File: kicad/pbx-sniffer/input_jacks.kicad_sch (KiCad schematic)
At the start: 24 parts

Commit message: commenced placement on pcb
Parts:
- renumbered J7 to J1, J4 to J10, J5 to J11, J6 to J12, J8 to J2, J9 to J3, J10 to J4, J11 to J5, J12 to J6, J1 to J7, J2 to J8, J3 to J9
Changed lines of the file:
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@@
+		(on_board yes)
+		(dnp no)
+		(property "Reference" "J2"
+			(at 81.28 53.34 0)
+			(effects
+				(font
+					(size 1.27 1.27)
+				)
+			)
+		)
+		(property "Value" "~"
+			(at 80.01 52.07 0)
+			(effects
+				(font
+					(size 1.27 1.27)
+				)
+				(hide yes)
+			)
+		)
+		(property "Footprint" "Phones:Molex 0955016649"
+			(at 81.28 54.61 0)
+			(effects
+				(font
+					(size 1.27 1.27)
+				)
+				(hide yes)
+			)
+		)
+		(property "Datasheet" ""
+			(at 81.28 54.61 0)
+			(effects
+				(font
+					(size 1.27 1.27)
+				)
+				(hide yes)
+			)
+		)
+		(property "Description" ""
+			(at 81.28 54.61 0)
+			(effects
+				(font
+					(size 1.27 1.27)
+				)
+				(hide yes)
+			)
+		)
+		(property "DKPN" "WM5574-ND"
+			(at 81.28 54.61 0)
+			(effects
+				(font
+					(size 1.27 1.27)
+				)
+				(hide yes)
+			)
+		)
+		(pin "4"
+		)
+		(pin "3"
+		)
+		(pin "2"
+		)
+		(pin "1"
+		)
+		(instances
+			(project "pbx-sniffer"
+				(path "/4a5b9b8a-323a-4796-bf73-ccba532d2e31/7f66e062-f194-4d68-9744-df7dfe6719d2"
+					(reference "J2")
+					(unit 1)
+				)
+			)
+		)
+	)
+	(symbol
+		(lib_id "Phones:Jack 6P4C RJ11")
+		(at 85.09 54.61 0)
+		(unit 1)
+		(exclude_from_sim no)
+		(in_bom yes)
 		(on_board yes)
 		(dnp no)
 		(property "Reference" "J8"
-			(at 81.28 53.34 0)
-			(effects
-				(font
-					(size 1.27 1.27)
-				)
-			)
-		)
-		(property "Value" "~"
-			(at 80.01 52.07 0)
-			(effects
-				(font
-					(size 1.27 1.27)
-				)
-				(hide yes)
-			)
-		)
-		(property "Footprint" "Phones:Molex 0955016649"
-			(at 81.28 54.61 0)
-			(effects
-				(font
-					(size 1.27 1.27)
-				)
-				(hide yes)
-			)
-		)
-		(property "Datasheet" ""
-			(at 81.28 54.61 0)
-			(effects
-				(font
-					(size 1.27 1.27)
-				)
-				(hide yes)
-			)
-		)
-		(property "Description" ""
-			(at 81.28 54.61 0)
-			(effects
-				(font
-					(size 1.27 1.27)
-				)
-				(hide yes)
-			)
-		)
-		(property "DKPN" "WM5574-ND"
-			(at 81.28 54.61 0)
+			(at 85.09 53.34 0)
+			(effects
+				(font
+					(size 1.27 1.27)
+				)
+			)
+		)
+		(property "Value" "~"
+			(at 86.36 52.07 0)
+			(effects
+				(font
+					(size 1.27 1.27)
+				)
+				(hide yes)
+			)
+		)
+		(property "Footprint" "Phones:Molex 0955016649"
+			(at 85.09 54.61 0)
+			(effects
+				(font
+					(size 1.27 1.27)
+				)
+				(hide yes)
+			)
+		)
+		(property "Datasheet" ""
+			(at 85.09 54.61 0)
+			(effects
+				(font
+					(size 1.27 1.27)
+				)
+				(hide yes)
+			)
+		)
+		(property "Description" ""
+			(at 85.09 54.61 0)
+			(effects
+				(font
+					(size 1.27 1.27)
+				)
+				(hide yes)
+			)
+		)
+		(property "DKPN" "WM5574-ND"
+			(at 85.09 54.61 0)
 			(effects
 				(font
@@
 				(path "/4a5b9b8a-323a-4796-bf73-ccba532d2e31/7f66e062-f194-4d68-9744-df7dfe6719d2"
 					(reference "J8")
-					(unit 1)
-				)
-			)
-		)
-	)
-	(symbol
-		(lib_id "Phones:Jack 6P4C RJ11")
-		(at 85.09 54.61 0)
-		(unit 1)
-		(exclude_from_sim no)
-		(in_bom yes)
-		(on_board yes)
-		(dnp no)
-		(property "Reference" "J2"
-			(at 85.09 53.34 0)
-			(effects
-				(font
-					(size 1.27 1.27)
-				)
-			)
-		)
-		(property "Value" "~"
-			(at 86.36 52.07 0)
-			(effects
-				(font
-					(size 1.27 1.27)
-				)
-				(hide yes)
-			)
-		)
-		(property "Footprint" "Phones:Molex 0955016649"
-			(at 85.09 54.61 0)
-			(effects
-				(font
-					(size 1.27 1.27)
-				)
-				(hide yes)
-			)
-		)
-		(property "Datasheet" ""
-			(at 85.09 54.61 0)
-			(effects
-				(font
-					(size 1.27 1.27)
-				)
-				(hide yes)
-			)
-		)
-		(property "Description" ""
-			(at 85.09 54.61 0)
-			(effects
-				(font
-					(size 1.27 1.27)
-				)
-				(hide yes)
-			)
-		)
-		(property "DKPN" "WM5574-ND"
-			(at 85.09 54.61 0)
-			(effects
-				(font
-					(size 1.27 1.27)
-				)
-				(hide yes)
-			)
-		)
-		(pin "4"
-		)
-		(pin "3"
-		)
-		(pin "2"
-		)
-		(pin "1"
-		)
-		(instances
-			(project "pbx-sniffer"
-				(path "/4a5b9b8a-323a-4796-bf73-ccba532d2e31/7f66e062-f194-4d68-9744-df7dfe6719d2"
-					(reference "J2")
 					(unit 1)
 				)
@@
 		(on_board yes)
 		(dnp no)
-		(property "Reference" "J10"
+		(property "Reference" "J4"
 			(at 81.28 93.98 0)
 			(effects
@@
 			(project "pbx-sniffer"
 				(path "/4a5b9b8a-323a-4796-bf73-ccba532d2e31/7f66e062-f194-4d68-9744-df7dfe6719d2"
-					(reference "J10")
+					(reference "J4")
 					(unit 1)
 				)
@@
 		(on_board yes)
 		(dnp no)
-		(property "Reference" "J3"
+		(property "Reference" "J9"
 			(at 85.09 73.66 0)
 			(effects
@@
 			(project "pbx-sniffer"
 				(path "/4a5b9b8a-323a-4796-bf73-ccba532d2e31/7f66e062-f194-4d68-9744-df7dfe6719d2"
-					(reference "J3")
+					(reference "J9")
 					(unit 1)
 				)
@@
 		(on_board yes)
 		(dnp no)
-		(property "Reference" "J12"
+		(property "Reference" "J6"
 			(at 81.28 134.62 0)
 			(effects
@@
 			(project "pbx-sniffer"
 				(path "/4a5b9b8a-323a-4796-bf73-ccba532d2e31/7f66e062-f194-4d68-9744-df7dfe6719d2"
-					(reference "J12")
+					(reference "J6")
 					(unit 1)
 				)
@@
 		(on_board yes)
 		(dnp no)
-		(property "Reference" "J5"
+		(property "Reference" "J11"
 			(at 85.09 114.3 0)
 			(effects
@@
 			(project "pbx-sniffer"
 				(path "/4a5b9b8a-323a-4796-bf73-ccba532d2e31/7f66e062-f194-4d68-9744-df7dfe6719d2"
-					(reference "J5")
+					(reference "J11")
 					(unit 1)
 				)
@@
 		(on_board yes)
 		(dnp no)
-		(property "Reference" "J11"
+		(property "Reference" "J5"
 			(at 81.28 114.3 0)
 			(effects
@@
 			(project "pbx-sniffer"
 				(path "/4a5b9b8a-323a-4796-bf73-ccba532d2e31/7f66e062-f194-4d68-9744-df7dfe6719d2"
-					(reference "J11")
+					(reference "J5")
 					(unit 1)
 				)
@@
 		(on_board yes)
 		(dnp no)
-		(property "Reference" "J9"
+		(property "Reference" "J3"
 			(at 81.28 73.66 0)
 			(effects
@@
 			(project "pbx-sniffer"
 				(path "/4a5b9b8a-323a-4796-bf73-ccba532d2e31/7f66e062-f194-4d68-9744-df7dfe6719d2"
-					(reference "J9")
+					(reference "J3")
 					(unit 1)
 				)
@@
 		(on_board yes)
 		(dnp no)
-		(property "Reference" "J4"
+		(property "Reference" "J10"
 			(at 85.09 93.98 0)
 			(effects
@@
 			(project "pbx-sniffer"
 				(path "/4a5b9b8a-323a-4796-bf73-ccba532d2e31/7f66e062-f194-4d68-9744-df7dfe6719d2"
-					(reference "J4")
+					(reference "J10")
 					(unit 1)
 				)
@@
 		(on_board yes)
 		(dnp no)
-		(property "Reference" "J7"
+		(property "Reference" "J1"
 			(at 81.28 33.02 0)
 			(effects
@@
 			(project "pbx-sniffer"
 				(path "/4a5b9b8a-323a-4796-bf73-ccba532d2e31/7f66e062-f194-4d68-9744-df7dfe6719d2"
-					(reference "J7")
+					(reference "J1")
 					(unit 1)
 				)
@@
 		(on_board yes)
 		(dnp no)
-		(property "Reference" "J6"
+		(property "Reference" "J12"
 			(at 85.09 134.62 0)
 			(effects
@@
 			(project "pbx-sniffer"
 				(path "/4a5b9b8a-323a-4796-bf73-ccba532d2e31/7f66e062-f194-4d68-9744-df7dfe6719d2"
-					(reference "J6")
+					(reference "J12")
 					(unit 1)
 				)
@@
 		(on_board yes)
 		(dnp no)
-		(property "Reference" "J1"
+		(property "Reference" "J7"
 			(at 85.09 33.02 0)
 			(effects
@@
 			(project "pbx-sniffer"
 				(path "/4a5b9b8a-323a-4796-bf73-ccba532d2e31/7f66e062-f194-4d68-9744-df7dfe6719d2"
-					(reference "J1")
-					(unit 1)
-				)
+					(reference "J7")
+					(unit 1)
+				)

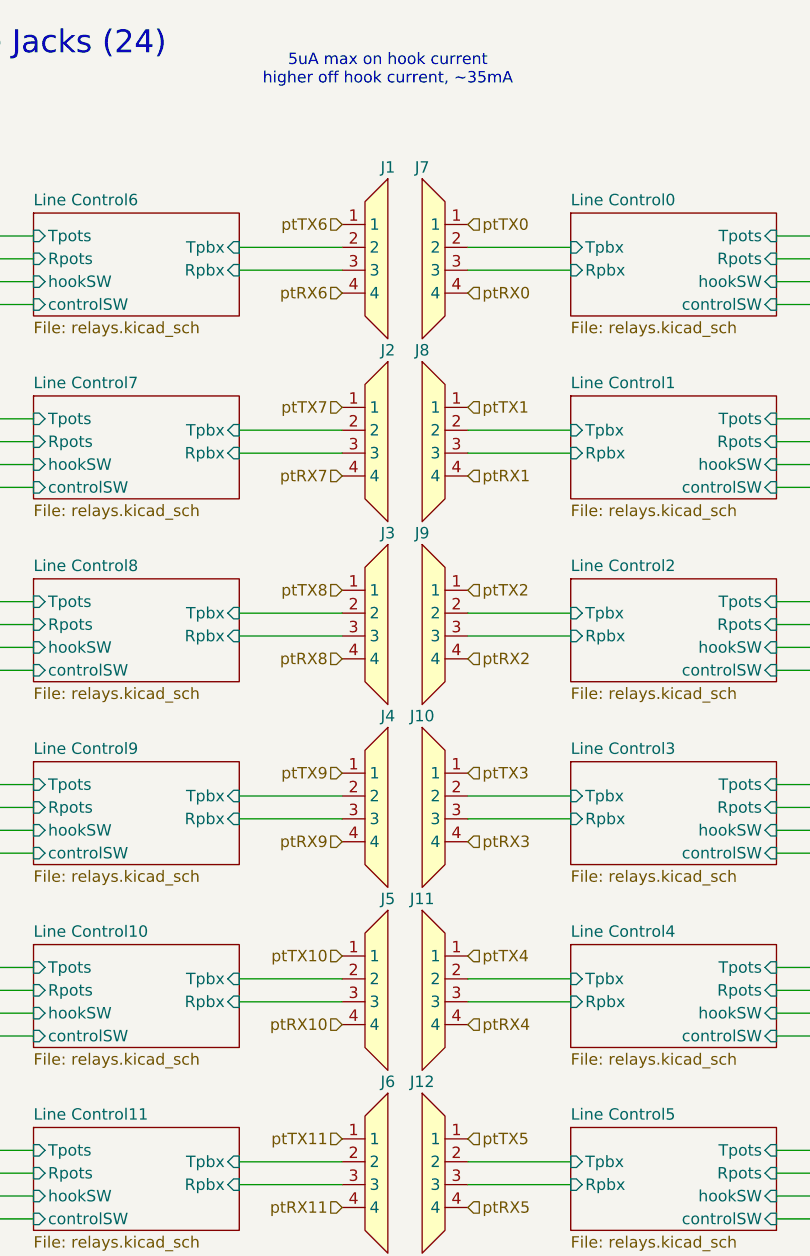
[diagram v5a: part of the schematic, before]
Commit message: initial module structure, for tiling later
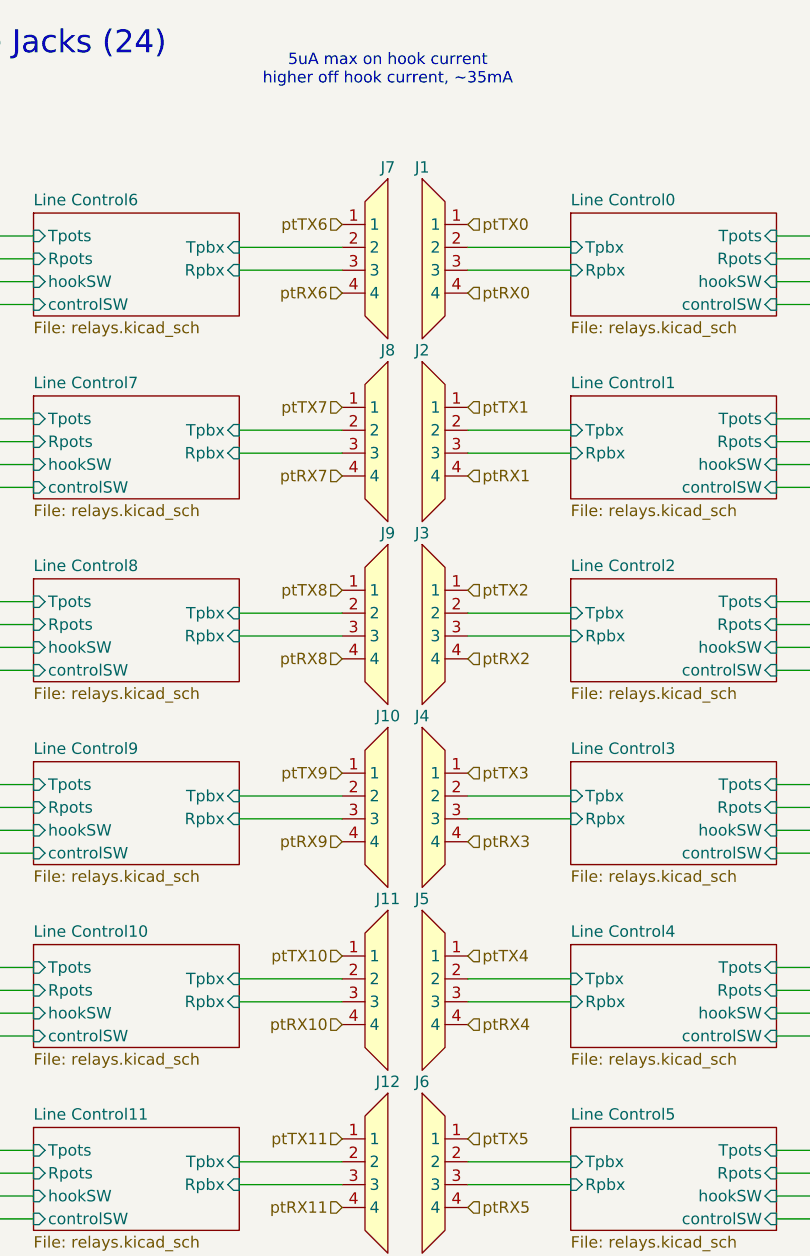
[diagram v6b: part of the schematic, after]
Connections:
- net Line Control0/Rpbx: now also J1.3; no longer J7.3
- net Line Control0/Tpbx: now also J1.2; no longer J7.2
- net Line Control1/Rpbx: now also J2.3; no longer J8.3
- net Line Control1/Tpbx: now also J2.2; no longer J8.2
- net Line Control10/Rpbx: now also J11.3; no longer J5.3
- net Line Control10/Tpbx: now also J11.2; no longer J5.2
- net Line Control11/Rpbx: now also J12.3; no longer J6.3
- net Line Control11/Tpbx: now also J12.2; no longer J6.2
- net Line Control2/Rpbx: now also J3.3; no longer J9.3
- net Line Control2/Tpbx: now also J3.2; no longer J9.2
- net Line Control3/Rpbx: now also J4.3; no longer J10.3
- net Line Control3/Tpbx: now also J4.2; no longer J10.2
- net Line Control4/Rpbx: now also J5.3; no longer J11.3
- net Line Control4/Tpbx: now also J5.2; no longer J11.2
- net Line Control5/Rpbx: now also J6.3; no longer J12.3
- net Line Control5/Tpbx: now also J6.2; no longer J12.2
- net Line Control6/Rpbx: now also J7.3; no longer J1.3
- net Line Control6/Tpbx: now also J7.2; no longer J1.2
- net Line Control7/Rpbx: now also J8.3; no longer J2.3
- net Line Control7/Tpbx: now also J8.2; no longer J2.2
- net Line Control8/Rpbx: now also J9.3; no longer J3.3
- net Line Control8/Tpbx: now also J9.2; no longer J3.2
- net Line Control9/Rpbx: now also J10.3; no longer J4.3
- net Line Control9/Tpbx: now also J10.2; no longer J4.2
- net ptRX0: now also J1.4; no longer J7.4
- net ptRX1: now also J2.4; no longer J8.4
- net ptRX10: now also J11.4; no longer J5.4
- net ptRX11: now also J12.4; no longer J6.4
- net ptRX2: now also J3.4; no longer J9.4
- net ptRX3: now also J4.4; no longer J10.4
- net ptRX4: now also J5.4; no longer J11.4
- net ptRX5: now also J6.4; no longer J12.4
- net ptRX6: now also J7.4; no longer J1.4
- net ptRX7: now also J8.4; no longer J2.4
- net ptRX8: now also J9.4; no longer J3.4
- net ptRX9: now also J10.4; no longer J4.4
- net ptTX0: now also J1.1; no longer J7.1
- net ptTX1: now also J2.1; no longer J8.1
- net ptTX10: now also J11.1; no longer J5.1
- net ptTX11: now also J12.1; no longer J6.1
- net ptTX2: now also J3.1; no longer J9.1
- net ptTX3: now also J4.1; no longer J10.1
- net ptTX4: now also J5.1; no longer J11.1
- net ptTX5: now also J6.1; no longer J12.1
- net ptTX6: now also J7.1; no longer J1.1
- net ptTX7: now also J8.1; no longer J2.1
- net ptTX8: now also J9.1; no longer J3.1
- net ptTX9: now also J10.1; no longer J4.1
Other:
- moved on the sheet: J1, J10, J11, J12, J2, J3, J4, J5, J6, J7, J8, J9

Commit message: update to kicad 10 & fix nucleo symbol to use background color
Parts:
- J1, J10, J11, J12, J13, J14, J15, J16, J17, J18, J19, J2, J20, J21, J22, J23, J24, J3, J4, J5, J6, J7, J8, J9: value ~ -> (none)
